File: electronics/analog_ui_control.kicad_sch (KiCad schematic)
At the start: 2 parts, among them J10 Conn_01x08, U22 LM339_4ch

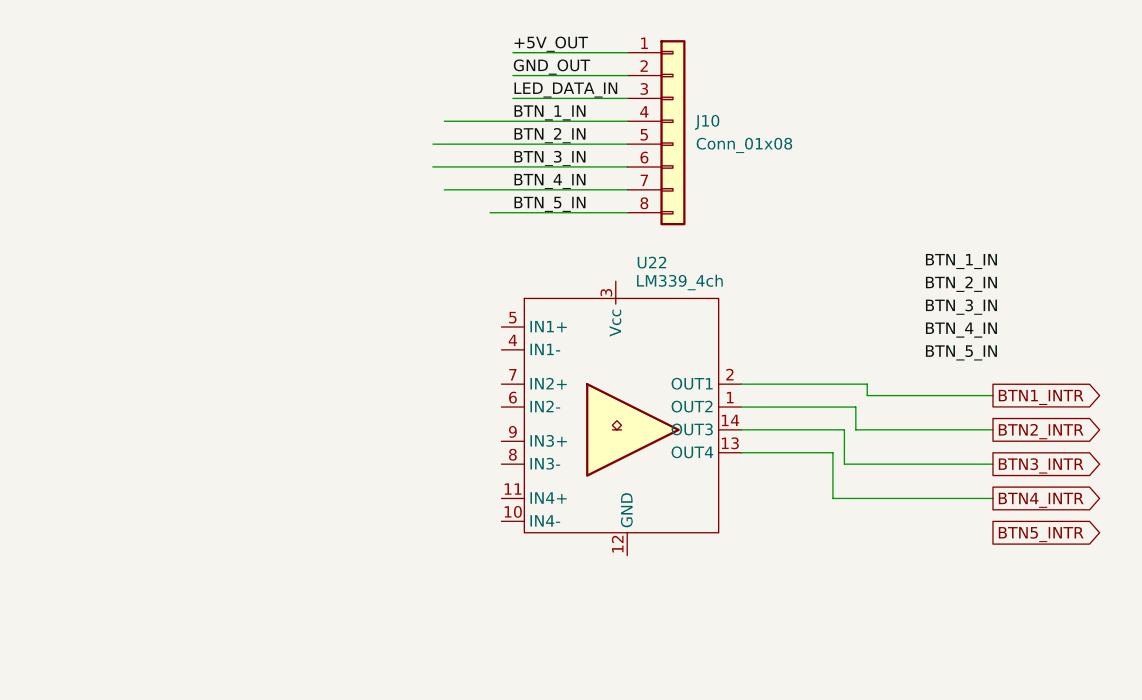
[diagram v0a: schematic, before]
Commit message: start to create BOM and finalising symbol fields
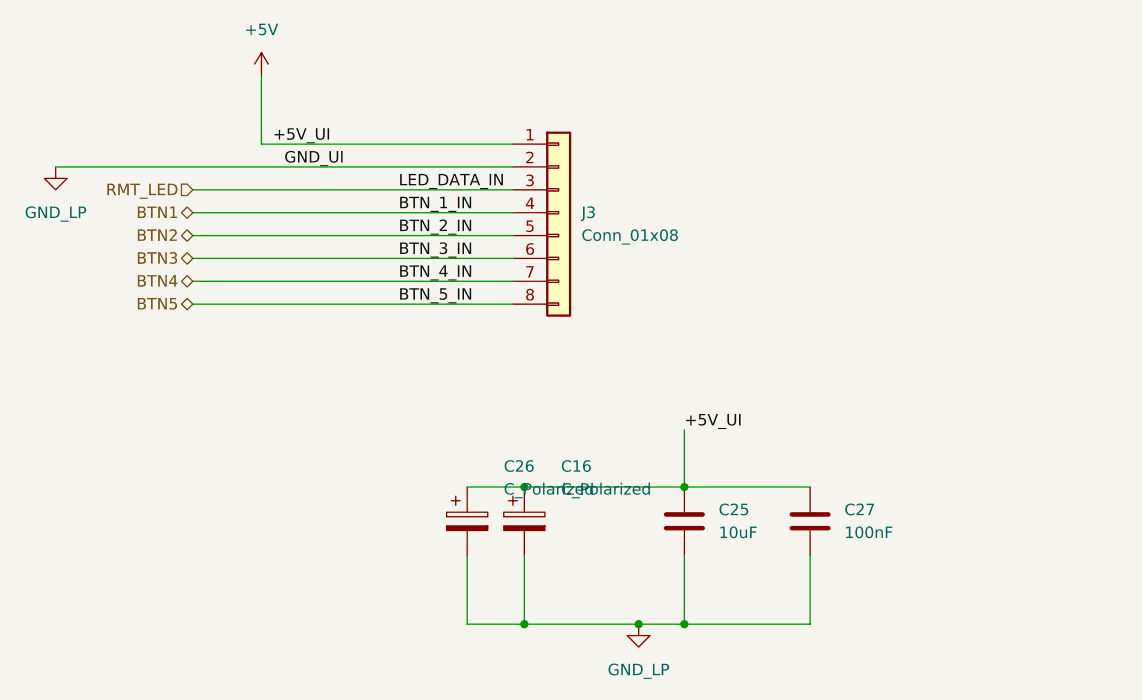
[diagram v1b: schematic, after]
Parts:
- removed J10: Conn_01x08, TerminalBlock:TerminalBlock_Xinya_XY308-2.54-8P_1x08_P2.54mm_Horizontal, symbol Connector_Generic:Conn_01x08
- removed U22: LM339_4ch, Package_SO:HTSSOP-14-1EP_4.4x5mm_P0.65mm_EP3.4x5mm_Mask3x3.1mm_ThermalVias, symbol HeavyDuty:LM339_4ch
- added C16, C26: C_Polarized, Capacitor_THT:CP_Radial_D5.0mm_P2.50mm, symbol Device:C_Polarized
- added C25: 10uF, Capacitor_SMD:C_0805_2012Metric, symbol Device:C
- added C27: 100nF, Capacitor_SMD:C_0805_2012Metric, symbol Device:C
- added J3: Conn_01x08, TerminalBlock:TerminalBlock_Xinya_XY308-2.54-8P_1x08_P2.54mm_Horizontal, symbol Connector_Generic:Conn_01x08
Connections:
- new net +5V: C16.1, C25.2, C26.1, C27.2, J3.1 (Pin_1)
- new net BTN1: J3.4 (Pin_4)
- new net BTN2: J3.5 (Pin_5)
- new net BTN3: J3.6 (Pin_6)
- new net BTN4: J3.7 (Pin_7)
- new net BTN5: J3.8 (Pin_8)
- new net GND_LP: C16.2, C25.1, C26.2, C27.1, J3.2 (Pin_2)
- new net RMT_LED: J3.3 (Pin_3)
